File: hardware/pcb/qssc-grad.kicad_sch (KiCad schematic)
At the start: 134 parts, among them J1 FT232RL, J10 USB-C, J12 BTB_HOST, J2 5V Barrel, J3 SMA, J4 12V LED, J7 RESET, J8 MW_GATE, J9 JTAG, U1 XC7A35T-1CSG324C, U3 ADF4351BCPZ, U5 GVA-84+, U8 W25Q128JVSIQ, Y1 100MHz XO

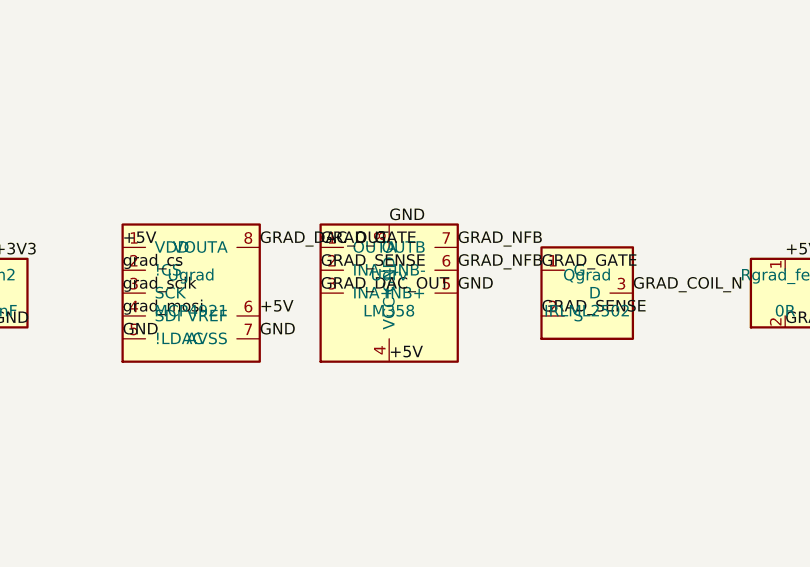
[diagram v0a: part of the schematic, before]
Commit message: fix(hardware): LM358 V-/V+ swap, MPN repairs, full grad copper repair, gate re-pins
- LM358 library symbol pins: 4 VCC->V-, 8 GND->V+ (real LM358 pinout)
- grad SCH: +5V/GND labels swapped at the UDRV pins; board pads swapped to
  match (Udrv pad 4 = GND, pad 8 = +5V); schematic_parity 0 in kicad-cli DRC
- BOM: J9 61300411121 -> 61301011121 (2x05 needs 10 contacts), Udrv
  LM358P -> LM358DR; the BOM delta pin (test_dumb_mistakes) re-pinned to
  exactly the reviewed 2 removes / 3 adds (issues #168/#169)
- grad PCB: all 12 formerly stranded cluster pads routed (net 6 +5V: 12
  F.Cu segments incl. the Rgrad_feed west route and the north-edge bridge
  to the existing +5V via at (114.04, 5.11); net 18 GND: 15 F.Cu segments;
  net 24 GRAD_SENSE: 2). No new via: the planned through-via at (139.5,
  94.8) was retracted after a ray-cast point-in-polygon check showed it
  inside the committed In1 (GND) and In2 (+3V3) pours -- the F.Cu-only
  bridge keeps both inner planes intact, no zone refill needed.
- electrical sanity: the four repaired gates re-pinned green (markers
  dropped); the MCP4921 VDD xfail stays (defect 3 open)
- DRC (kicad-cli): 0 violations, 0 unconnected, 0 schematic parity; full
  suite captures show exactly one failing test (known pre-existing C87
  placement, test_bom_matches_board[main]) and no unexpected XPASS

[skip ci]

Co-Authored-By: Claude <noreply@anthropic.com>
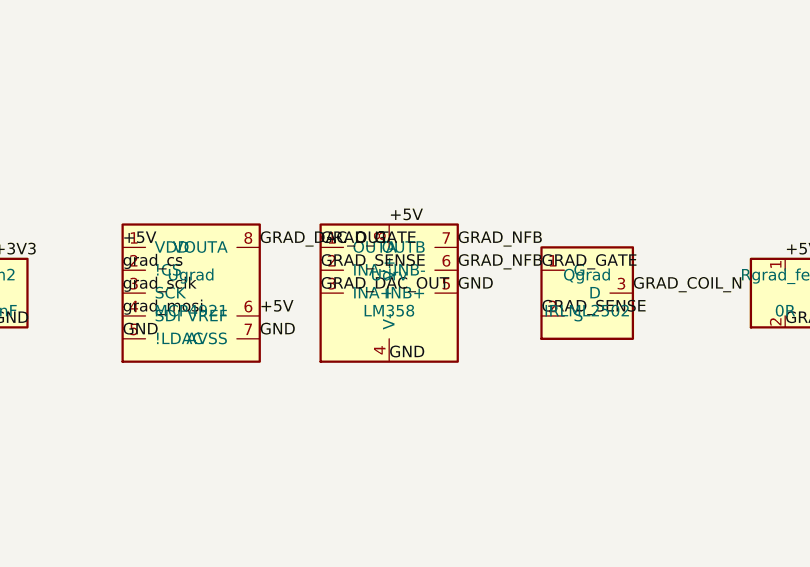
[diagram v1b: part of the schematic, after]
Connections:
- net +5V: now also Udrv.8 (V+); no longer Udrv.4 (VCC)
- net GND: now also Udrv.4 (V-); no longer Udrv.8 (GND)
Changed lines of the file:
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@@
 		)
 	)
-	(label "+5V"
+	(label "GND"
 		(at 640.0 27.62 0)
 		(fields_autoplaced yes)
@@
 		)
 	)
-	(label "GND"
+	(label "+5V"
 		(at 640.0 12.38 0)
 		(fields_autoplaced yes)
